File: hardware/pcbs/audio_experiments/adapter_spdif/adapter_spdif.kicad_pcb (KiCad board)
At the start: 2 copper layers, 35 x 33 mm, 15 parts, among them J1 Header_Horizontal_01x04, J2 Conn_Coaxial_2x, U1 74HCU04

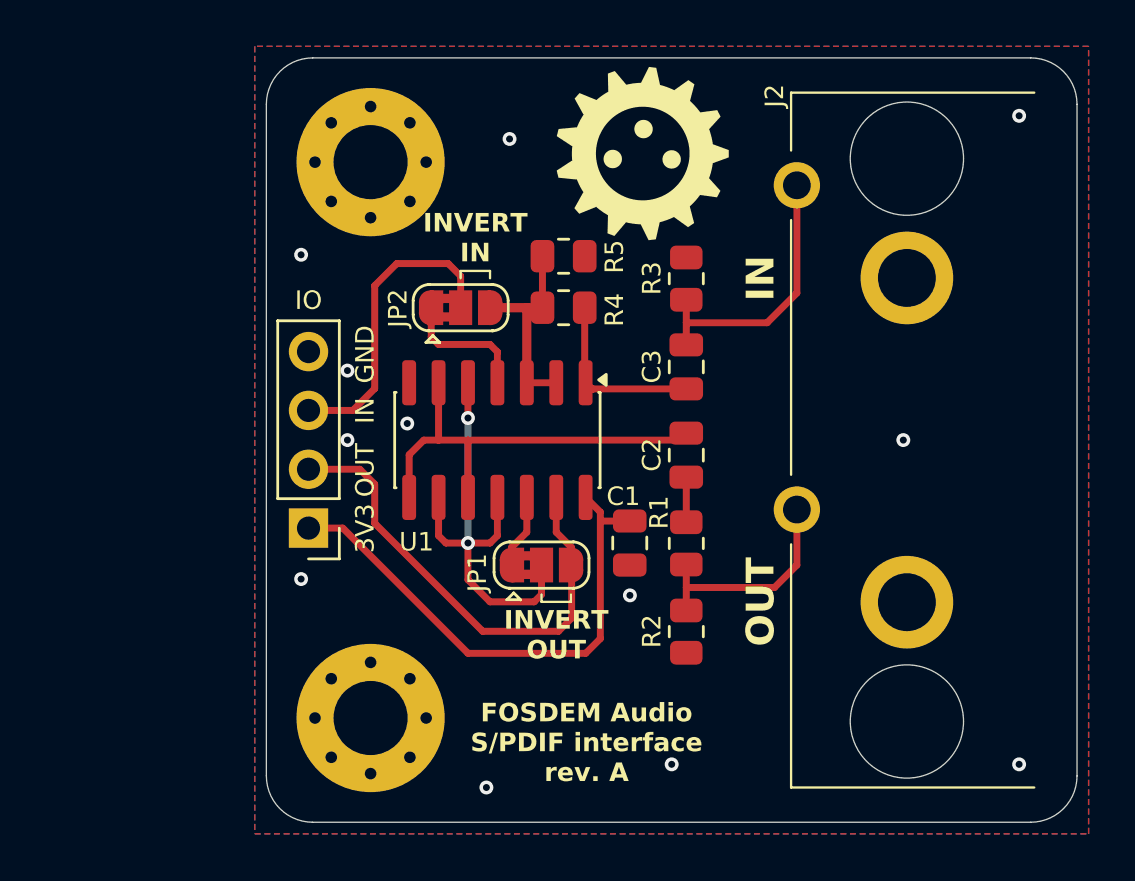
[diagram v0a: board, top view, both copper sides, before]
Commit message: rearrange addon header
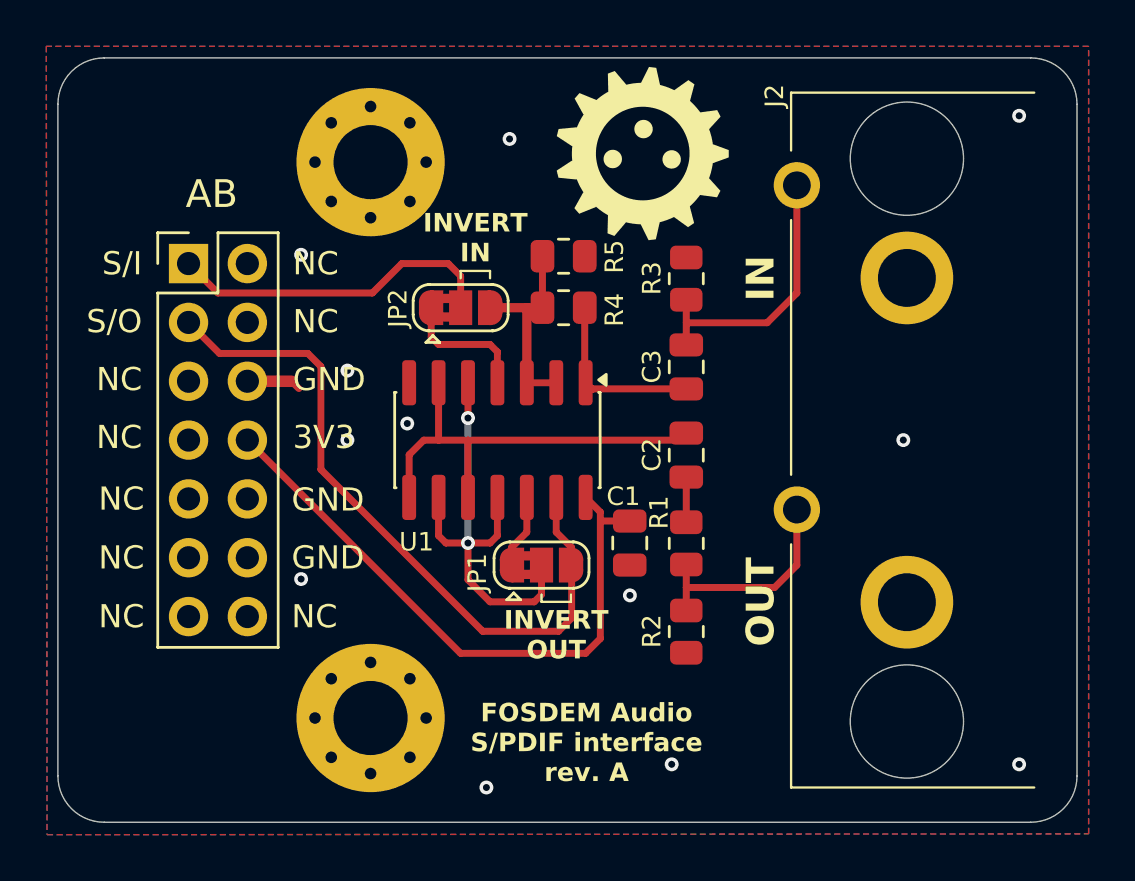
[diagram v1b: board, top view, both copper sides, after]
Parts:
- J1: value Header_Horizontal_01x04 -> Conn_02x07_Odd_Even; footprint conn:PinHeader_1x04_P2.54mm_Vertical -> conn:PinHeader_2x07_P2.54mm_Vertical
- moved J1 12.5 mm to (-22.9, -7.62), turned to 0 degrees
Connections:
- J1 pad 1: +3.3V -> /SPDIF In/SPDIF_IN_LOG
- J1 pad 2: /SPDIF Out/SPDIF_OUT_LOG -> unconnected-(J1-Pin_2-Pad2)
- J1 pad 3: /SPDIF In/SPDIF_IN_LOG -> /SPDIF Out/SPDIF_OUT_LOG
- J1 pad 4: GND -> unconnected-(J1-Pin_4-Pad4)
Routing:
- net /SPDIF Out/SPDIF_OUT_LOG: track 21.0 -> 30.4 mm
- net +3.3V: track 22.7 -> 26.9 mm
- net GND: track 0.00 -> 2.35 mm
- net /SPDIF In/SPDIF_IN_LOG: track 13.4 -> 14.4 mm
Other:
- board size 35 x 33 mm -> 44 x 33 mm

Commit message: minor changes
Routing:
- net +3.3V: track 26.9 -> 28.0 mm
- net /SPDIF Out/SPDIF_OUT_LOG: track 30.4 -> 31.0 mm
- net GND: vias 12 -> 13
